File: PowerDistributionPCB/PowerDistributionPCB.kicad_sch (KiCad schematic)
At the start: 38 parts, among them J1 USB3_A, Q1 AOD4185, U1 AP63203WU

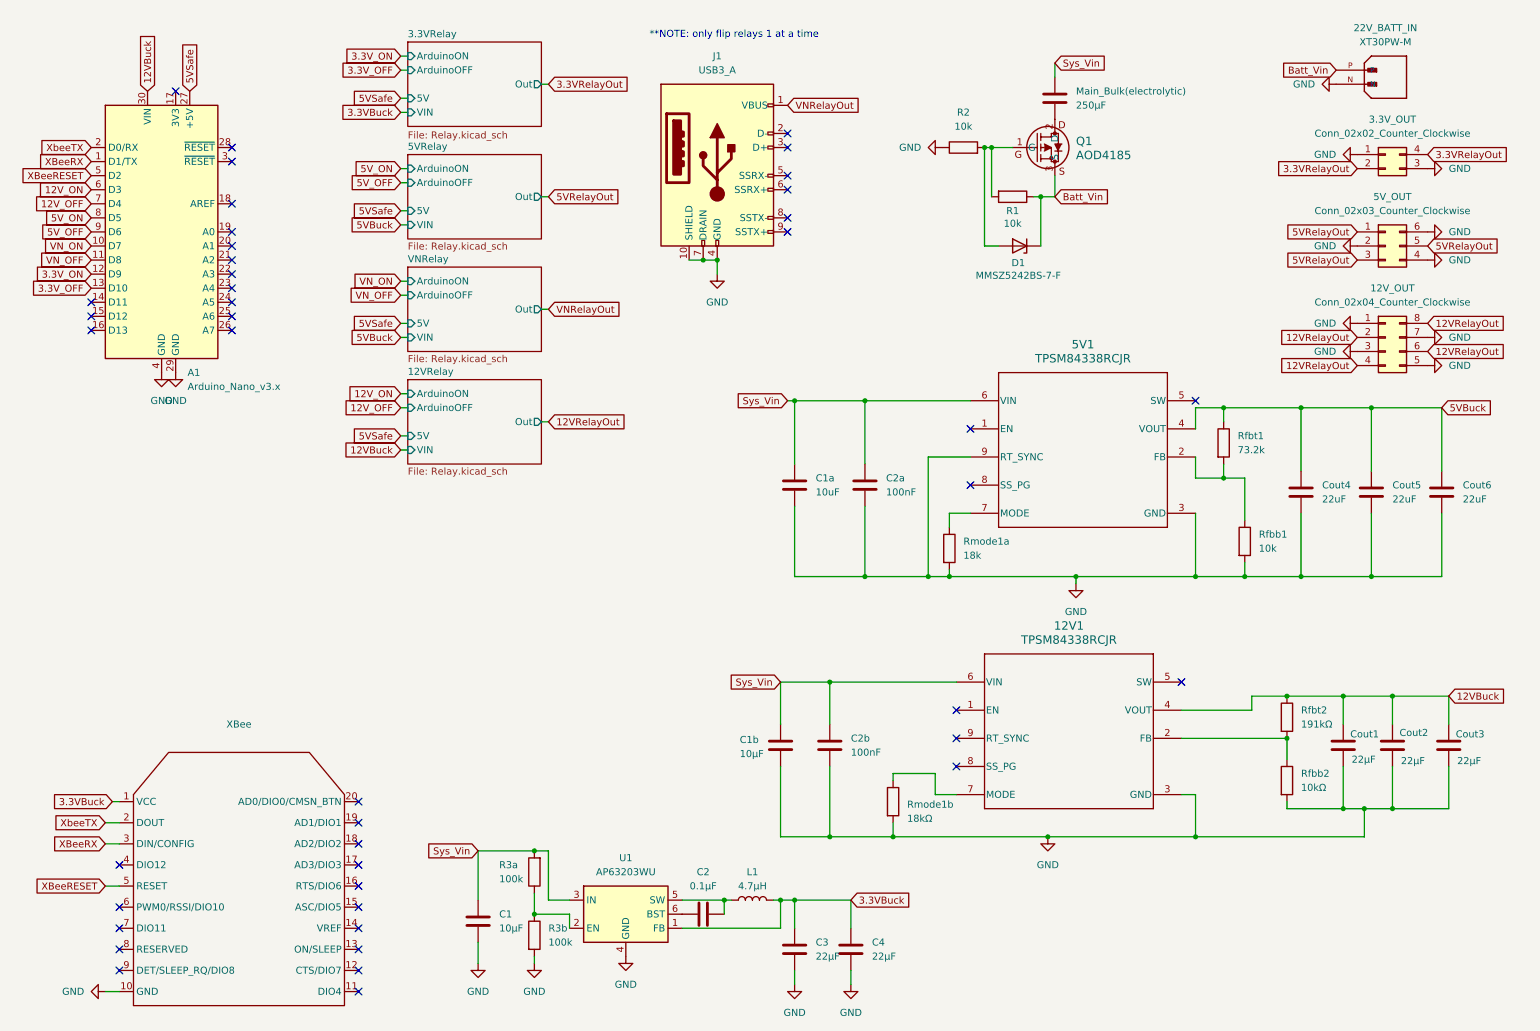
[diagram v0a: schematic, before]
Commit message: started adding footprints
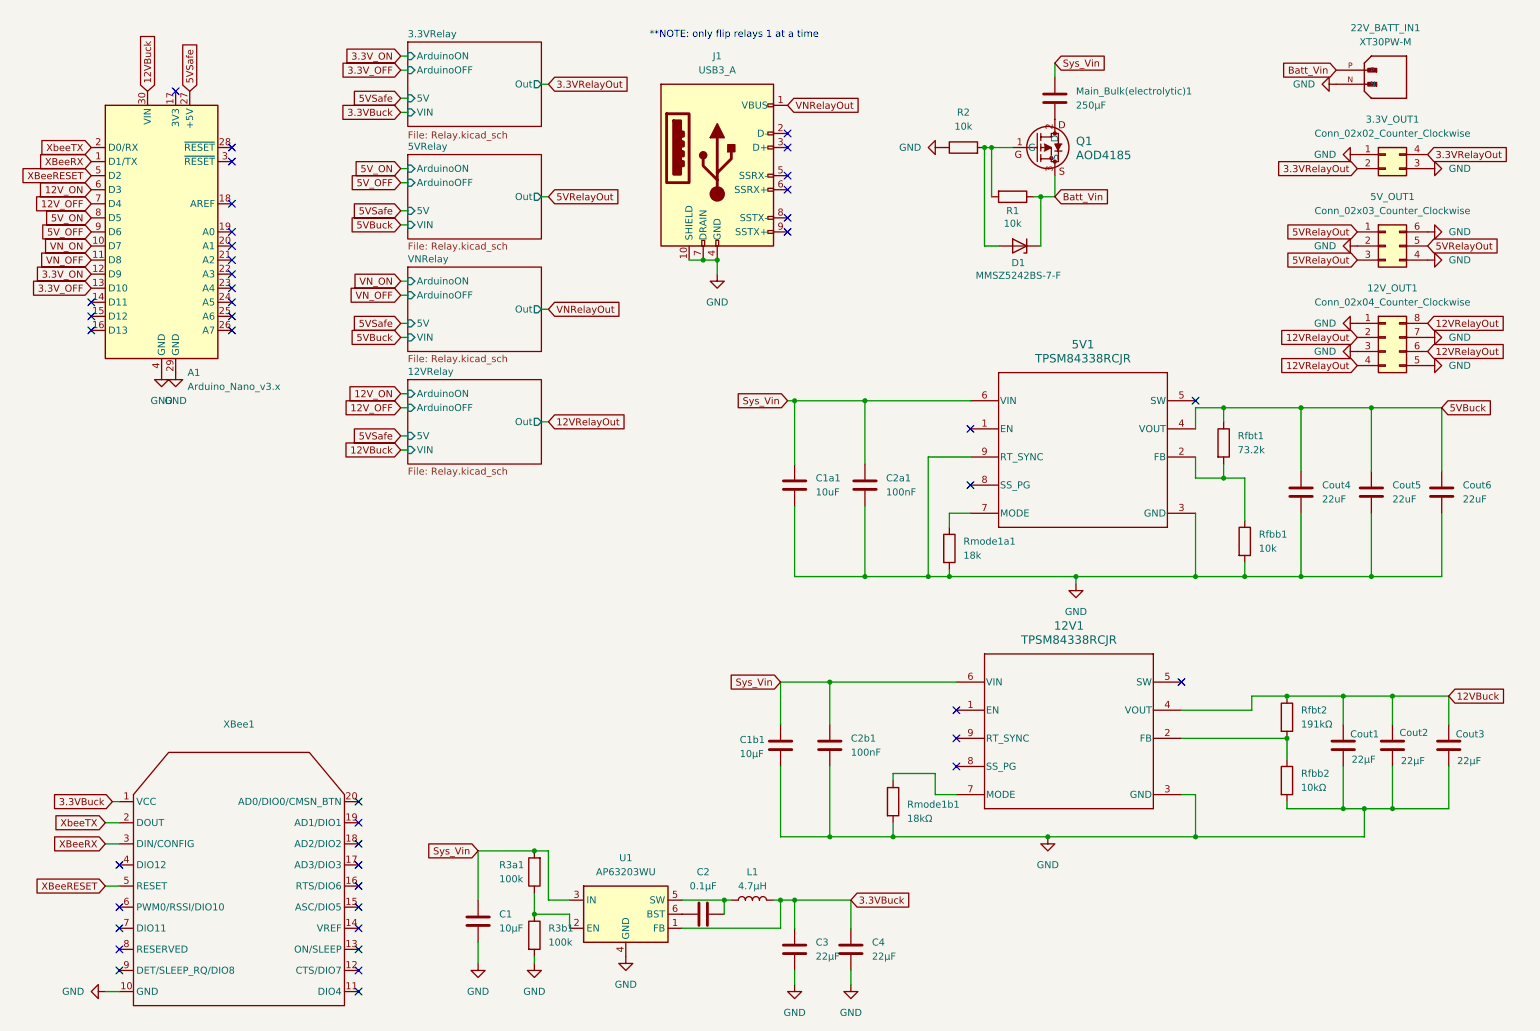
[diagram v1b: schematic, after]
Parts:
- C1a1: renamed from C1a; footprint (none) -> Capacitor_SMD:C_1210_3225Metric_Pad1.33x2.70mm_HandSolder
- C1b1: renamed from C1b; footprint (none) -> Capacitor_SMD:C_1210_3225Metric_Pad1.33x2.70mm_HandSolder
- C2a1: renamed from C2a; footprint (none) -> Capacitor_SMD:C_01005_0402Metric_Pad0.57x0.30mm_HandSolder
- C2b1: renamed from C2b; footprint (none) -> Capacitor_SMD:C_01005_0402Metric_Pad0.57x0.30mm_HandSolder
- Cout1, Cout2, Cout3: footprint (none) -> Capacitor_SMD:C_1210_3225Metric_Pad1.33x2.70mm_HandSolder
- Cout4, Cout5, Cout6: footprint (none) -> Capacitor_SMD:C_1206_3216Metric_Pad1.33x1.80mm_HandSolder
- Rfbb1, Rfbb2, Rfbt1, Rfbt2: footprint (none) -> Capacitor_SMD:C_01005_0402Metric_Pad0.57x0.30mm_HandSolder
- Rmode1a1: renamed from Rmode1a; footprint (none) -> Capacitor_SMD:C_0201_0603Metric_Pad0.64x0.40mm_HandSolder
- Rmode1b1: renamed from Rmode1b; footprint (none) -> Capacitor_SMD:C_0201_0603Metric_Pad0.64x0.40mm_HandSolder
- XBee1: renamed from XBee; footprint (none) -> CUSail:XBee
- renumbered 12V_OUT to 12V_OUT1, 22V_BATT_IN to 22V_BATT_IN1, 3.3V_OUT to 3.3V_OUT1, 5V_OUT to 5V_OUT1, Main_Bulk(electrolytic) to Main_Bulk(electrolytic)1, R3a to R3a1, R3b to R3b1
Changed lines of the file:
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@@
 			)
 		)
-		(property "Footprint" ""
+		(property "Footprint" "Capacitor_SMD:C_1210_3225Metric_Pad1.33x2.70mm_HandSolder"
 			(at 262.5852 147.32 0)
 			(effects
@@
 		(dnp no)
 		(fields_autoplaced yes)
-		(property "Reference" "XBee"
+		(property "Reference" "XBee1"
 			(at 53.34 139.7 0)
 			(effects
@@
 			)
 		)
-		(property "Footprint" ""
+		(property "Footprint" "CUSail:XBee"
 			(at 52.07 161.29 0)
 			(effects
@@
 			(project ""
 				(path "/b27c75df-6223-4cc6-be69-062c2b02d5c6"
-					(reference "XBee")
+					(reference "XBee1")
 					(unit 1)
 				)
@@
 			)
 		)
-		(property "Footprint" ""
+		(property "Footprint" "Capacitor_SMD:C_01005_0402Metric_Pad0.57x0.30mm_HandSolder"
 			(at 233.172 106.68 90)
 			(effects
@@
 		(on_board yes)
 		(dnp no)
-		(property "Reference" "C1b"
+		(property "Reference" "C1b1"
 			(at 143.764 142.494 0)
 			(effects
@@
 			)
 		)
-		(property "Footprint" ""
+		(property "Footprint" "Capacitor_SMD:C_1210_3225Metric_Pad1.33x2.70mm_HandSolder"
 			(at 152.0952 147.32 0)
 			(effects
@@
 			(project ""
 				(path "/b27c75df-6223-4cc6-be69-062c2b02d5c6"
-					(reference "C1b")
+					(reference "C1b1")
 					(unit 1)
 				)
@@
 		(dnp no)
 		(fields_autoplaced yes)
-		(property "Reference" "C1a"
+		(property "Reference" "C1a1"
 			(at 157.48 95.2499 0)
 			(effects
@@
 			)
 		)
-		(property "Footprint" ""
+		(property "Footprint" "Capacitor_SMD:C_1210_3225Metric_Pad1.33x2.70mm_HandSolder"
 			(at 154.6352 100.33 0)
 			(effects
@@
 			(project "PowerDistributionPCB"
 				(path "/b27c75df-6223-4cc6-be69-062c2b02d5c6"
-					(reference "C1a")
+					(reference "C1a1")
 					(unit 1)
 				)
@@
 		(dnp no)
 		(fields_autoplaced yes)
-		(property "Reference" "Main_Bulk(electrolytic)"
+		(property "Reference" "Main_Bulk(electrolytic)1"
 			(at 204.47 25.3999 0)
 			(effects
@@
 			(project ""
 				(path "/b27c75df-6223-4cc6-be69-062c2b02d5c6"
-					(reference "Main_Bulk(electrolytic)")
+					(reference "Main_Bulk(electrolytic)1")
 					(unit 1)
 				)
@@
 			)
 		)
-		(property "Footprint" ""
+		(property "Footprint" "Capacitor_SMD:C_1206_3216Metric_Pad1.33x1.80mm_HandSolder"
 			(at 258.7752 101.6 0)
 			(effects
@@
 		(on_board yes)
 		(dnp no)
-		(property "Reference" "Rmode1b"
+		(property "Reference" "Rmode1b1"
 			(at 173.99 154.178 0)
 			(effects
@@
 			)
 		)
-		(property "Footprint" ""
+		(property "Footprint" "Capacitor_SMD:C_0201_0603Metric_Pad0.64x0.40mm_HandSolder"
 			(at 169.672 153.67 90)
 			(effects
@@
 			(project ""
 				(path "/b27c75df-6223-4cc6-be69-062c2b02d5c6"
-					(reference "Rmode1b")
+					(reference "Rmode1b1")
 					(unit 1)
 				)
@@
 		(dnp no)
 		(fields_autoplaced yes)
-		(property "Reference" "C2b"
+		(property "Reference" "C2b1"
 			(at 163.83 142.2399 0)
 			(effects
@@
 			)
 		)
-		(property "Footprint" ""
+		(property "Footprint" "Capacitor_SMD:C_01005_0402Metric_Pad0.57x0.30mm_HandSolder"
 			(at 160.9852 147.32 0)
 			(effects
@@
 			(project ""
 				(path "/b27c75df-6223-4cc6-be69-062c2b02d5c6"
-					(reference "C2b")
+					(reference "C2b1")
 					(unit 1)
 				)
@@
 		(on_board yes)
 		(dnp no)
-		(property "Reference" "22V_BATT_IN"
+		(property "Reference" "22V_BATT_IN1"
 			(at 260.35 13.97 0)
 			(effects
@@
 			(project ""
 				(path "/b27c75df-6223-4cc6-be69-062c2b02d5c6"
-					(reference "22V_BATT_IN")
+					(reference "22V_BATT_IN1")
 					(unit 1)
 				)
@@
 			)
 		)
-		(property "Footprint" ""
+		(property "Footprint" "Capacitor_SMD:C_1210_3225Metric_Pad1.33x2.70mm_HandSolder"
 			(at 253.6952 147.32 0)
 			(effects
@@
 			)
 		)
-		(property "Footprint" ""
+		(property "Footprint" "Capacitor_SMD:C_1210_3225Metric_Pad1.33x2.70mm_HandSolder"
 			(at 272.7452 147.32 0)
 			(effects
@@
 		(on_board yes)
 		(dnp no)
-		(property "Reference" "R3a"
+		(property "Reference" "R3a1"
 			(at 100.33 165.1 0)
 			(effects
@@
 			(project "PowerDistributionPCB"
 				(path "/b27c75df-6223-4cc6-be69-062c2b02d5c6"
-					(reference "R3a")
+					(reference "R3a1")
 					(unit 1)
 				)
@@
 			)
 		)
-		(property "Footprint" ""
+		(property "Footprint" "Capacitor_SMD:C_1206_3216Metric_Pad1.33x1.80mm_HandSolder"
 			(at 246.0752 101.6 0)
 			(effects
@@
 		(dnp no)
 		(fields_autoplaced yes)
-		(property "Reference" "12V_OUT"
+		(property "Reference" "12V_OUT1"
 			(at 261.62 60.96 0)
 			(effects
@@
 			(project ""
 				(path "/b27c75df-6223-4cc6-be69-062c2b02d5c6"
-					(reference "12V_OUT")
+					(reference "12V_OUT1")
 					(unit 1)
 				)
@@
 			)
 		)
-		(property "Footprint" ""
+		(property "Footprint" "Capacitor_SMD:C_01005_0402Metric_Pad0.57x0.30mm_HandSolder"
 			(at 240.792 149.86 90)
 			(effects
@@
 		(dnp no)
 		(fields_autoplaced yes)
-		(property "Reference" "R3b"
+		(property "Reference" "R3b1"
 			(at 109.22 176.5299 0)
 			(effects
@@
 			(project "PowerDistributionPCB"
 				(path "/b27c75df-6223-4cc6-be69-062c2b02d5c6"
-					(reference "R3b")
+					(reference "R3b1")
 					(unit 1)
 				)
@@
 		(dnp no)
 		(fields_autoplaced yes)
-		(property "Reference" "Rmode1a"
+		(property "Reference" "Rmode1a1"
 			(at 184.15 106.6799 0)
 			(effects
@@
 			)
 		)
-		(property "Footprint" ""
+		(property "Footprint" "Capacitor_SMD:C_0201_0603Metric_Pad0.64x0.40mm_HandSolder"
 			(at 179.832 107.95 90)
 			(effects
@@
 			(project "PowerDistributionPCB"
 				(path "/b27c75df-6223-4cc6-be69-062c2b02d5c6"
-					(reference "Rmode1a")
+					(reference "Rmode1a1")
 					(unit 1)
 				)
@@
 		(dnp no)
 		(fields_autoplaced yes)
-		(property "Reference" "C2a"
+		(property "Reference" "C2a1"
 			(at 170.18 95.2499 0)
 			(effects
@@
 			)
 		)
-		(property "Footprint" ""
+		(property "Footprint" "Capacitor_SMD:C_01005_0402Metric_Pad0.57x0.30mm_HandSolder"
 			(at 167.3352 100.33 0)
 			(effects
@@
 			(project "PowerDistributionPCB"
 				(path "/b27c75df-6223-4cc6-be69-062c2b02d5c6"
-					(reference "C2a")
+					(reference "C2a1")
 					(unit 1)
 				)
@@
 			)
 		)
-		(property "Footprint" ""
+		(property "Footprint" "Capacitor_SMD:C_01005_0402Metric_Pad0.57x0.30mm_HandSolder"
 			(at 229.362 88.9 90)
 			(effects
@@
 			)
 		)
-		(property "Footprint" ""
+		(property "Footprint" "Capacitor_SMD:C_1206_3216Metric_Pad1.33x1.80mm_HandSolder"
 			(at 271.4752 101.6 0)
 			(effects
@@
 			)
 		)
-		(property "Footprint" ""
+		(property "Footprint" "Capacitor_SMD:C_01005_0402Metric_Pad0.57x0.30mm_HandSolder"
 			(at 240.792 138.43 90)
 			(effects
@@
 		(dnp no)
 		(fields_autoplaced yes)
-		(property "Reference" "3.3V_OUT"
+		(property "Reference" "3.3V_OUT1"
 			(at 261.62 30.48 0)
 			(effects
@@
 			(project ""
 				(path "/b27c75df-6223-4cc6-be69-062c2b02d5c6"
-					(reference "3.3V_OUT")
+					(reference "3.3V_OUT1")
 					(unit 1)
 				)
@@
 		(dnp no)
 		(fields_autoplaced yes)
-		(property "Reference" "5V_OUT"
+		(property "Reference" "5V_OUT1"
 			(at 261.62 44.45 0)
 			(effects
@@
 			(project ""
 				(path "/b27c75df-6223-4cc6-be69-062c2b02d5c6"
-					(reference "5V_OUT")
+					(reference "5V_OUT1")
 					(unit 1)
 				)

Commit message: more footprints on power board
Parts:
- 12V_OUT1: footprint (none) -> Connector_Molex:Molex_Mini-Fit_Jr_5566-08A_2x04_P4.20mm_Vertical
- 3.3V_OUT1: footprint (none) -> Connector_Molex:Molex_Mini-Fit_Jr_5566-04A_2x02_P4.20mm_Vertical
- 5V_OUT1: footprint (none) -> Connector_Molex:Molex_Mini-Fit_Jr_5566-06A_2x03_P4.20mm_Vertical
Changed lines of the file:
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@@
 			)
 		)
-		(property "Footprint" ""
+		(property "Footprint" "Connector_Molex:Molex_Mini-Fit_Jr_5566-08A_2x04_P4.20mm_Vertical"
 			(at 260.35 69.85 0)
 			(effects
@@
 			)
 		)
-		(property "Footprint" ""
+		(property "Footprint" "Connector_Molex:Molex_Mini-Fit_Jr_5566-04A_2x02_P4.20mm_Vertical"
 			(at 260.35 36.83 0)
 			(effects
@@
 			)
 		)
-		(property "Footprint" ""
+		(property "Footprint" "Connector_Molex:Molex_Mini-Fit_Jr_5566-06A_2x03_P4.20mm_Vertical"
 			(at 260.35 53.34 0)
 			(effects

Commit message: even more footprints
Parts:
- C1, C2, C3, C4, Main_Bulk(electrolytic)1: footprint (none) -> Capacitor_SMD:C_0201_0603Metric_Pad0.64x0.40mm_HandSolder
- R1, R2, R3a1, R3b1: footprint (none) -> Resistor_SMD:R_0805_2012Metric_Pad1.20x1.40mm_HandSolder
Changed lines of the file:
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@@
 			)
 		)
-		(property "Footprint" ""
+		(property "Footprint" "Resistor_SMD:R_0805_2012Metric_Pad1.20x1.40mm_HandSolder"
 			(at 193.04 42.672 90)
 			(effects
@@
 			)
 		)
-		(property "Footprint" ""
+		(property "Footprint" "Capacitor_SMD:C_0201_0603Metric_Pad0.64x0.40mm_HandSolder"
 			(at 201.6252 30.48 0)
 			(effects
@@
 			)
 		)
-		(property "Footprint" ""
+		(property "Footprint" "Capacitor_SMD:C_0201_0603Metric_Pad0.64x0.40mm_HandSolder"
 			(at 164.7952 184.15 0)
 			(effects
@@
 			)
 		)
-		(property "Footprint" ""
+		(property "Footprint" "Resistor_SMD:R_0805_2012Metric_Pad1.20x1.40mm_HandSolder"
 			(at 184.15 37.338 90)
 			(effects
@@
 			)
 		)
-		(property "Footprint" ""
+		(property "Footprint" "Resistor_SMD:R_0805_2012Metric_Pad1.20x1.40mm_HandSolder"
 			(at 108.458 166.37 90)
 			(effects
@@
 			)
 		)
-		(property "Footprint" ""
+		(property "Footprint" "Capacitor_SMD:C_0201_0603Metric_Pad0.64x0.40mm_HandSolder"
 			(at 140.97 173.0248 0)
 			(effects
@@
 			)
 		)
-		(property "Footprint" ""
+		(property "Footprint" "Resistor_SMD:R_0805_2012Metric_Pad1.20x1.40mm_HandSolder"
 			(at 104.902 177.8 90)
 			(effects
@@
 			)
 		)
-		(property "Footprint" ""
+		(property "Footprint" "Capacitor_SMD:C_0201_0603Metric_Pad0.64x0.40mm_HandSolder"
 			(at 97.4852 179.07 0)
 			(effects
@@
 			)
 		)
-		(property "Footprint" ""
+		(property "Footprint" "Capacitor_SMD:C_0201_0603Metric_Pad0.64x0.40mm_HandSolder"
 			(at 154.6352 184.15 0)
 			(effects

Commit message: assigned custom footprints
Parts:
- 12V1, 5V1: footprint RCJ0009A-MFG -> CUSail:TPSM84338RCJR
- Q1: footprint TO252_AOS -> CUSail:AOD4185
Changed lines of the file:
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@@
 			)
 		)
-		(property "Footprint" "RCJ0009A-MFG"
+		(property "Footprint" "CUSail:TPSM84338RCJR"
 			(at 182.88 130.81 0)
 			(effects
@@
 			)
 		)
-		(property "Footprint" "RCJ0009A-MFG"
+		(property "Footprint" "CUSail:TPSM84338RCJR"
 			(at 185.42 80.01 0)
 			(effects
@@
 			)
 		)
-		(property "Footprint" "TO252_AOS"
+		(property "Footprint" "CUSail:AOD4185"
 			(at 193.04 35.56 0)
 			(effects

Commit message: added even more custom footprints (and assigned)
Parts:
- 22V_BATT_IN1: footprint XT30PW-M:AMASS_XT30PW-M -> CUSail:XT30PW-M
- D1: footprint (none) -> CUSail:MMSZ5242BS-7-F
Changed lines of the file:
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@@
 			)
 		)
-		(property "Footprint" ""
+		(property "Footprint" "CUSail:MMSZ5242BS-7-F"
 			(at 194.31 53.34 0)
 			(effects
@@
 			)
 		)
-		(property "Footprint" "XT30PW-M:AMASS_XT30PW-M"
+		(property "Footprint" "CUSail:XT30PW-M"
 			(at 256.54 21.59 0)
 			(effects

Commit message: added inductor footprint
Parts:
- L1: footprint (none) -> CUSail:VLS4012
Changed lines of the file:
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@@
 			)
 		)
-		(property "Footprint" ""
+		(property "Footprint" "CUSail:VLS4012"
 			(at 146.05 171.45 0)
 			(effects

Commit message: finishing footprint stuff
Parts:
- C1: footprint Capacitor_SMD:C_0201_0603Metric_Pad0.64x0.40mm_HandSolder -> Capacitor_SMD:C_1206_3216Metric_Pad1.33x1.80mm_HandSolder
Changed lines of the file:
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@@
 			)
 		)
-		(property "Footprint" "Capacitor_SMD:C_0201_0603Metric_Pad0.64x0.40mm_HandSolder"
+		(property "Footprint" "Capacitor_SMD:C_1206_3216Metric_Pad1.33x1.80mm_HandSolder"
 			(at 97.4852 179.07 0)
 			(effects
